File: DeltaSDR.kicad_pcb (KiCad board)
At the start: 2 copper layers, 100 x 80 mm, 177 parts, among them J1 Conn_01x03_Male, J2 Conn_01x05_Male, J3 Barrel_Jack, J4 USB_A, J5 Conn_Coaxial, J6 Conn_01x02_Male, Q1 BSS123, Q2 BSS123, Q3 BSS123, Q4 BSS123, Q5 BSS123, Q6 BSS123, Q7 MMBT3904, T1 Transformer_1P_SS, T2 Transformer_1P_SS, U1 TC1262-33, U10 TLV2464CD, U11 SN74CBT3253, U12 MMG3H21NT1, U2 Si570, U3 SN74CBT3253, U4 PCM3060, U5 CY8C3246PVI-147, U6 TC1262-5, U7 TC1262-5, U8 74HC74, U9 LT6231CSB, Y1 Crystal_GND24

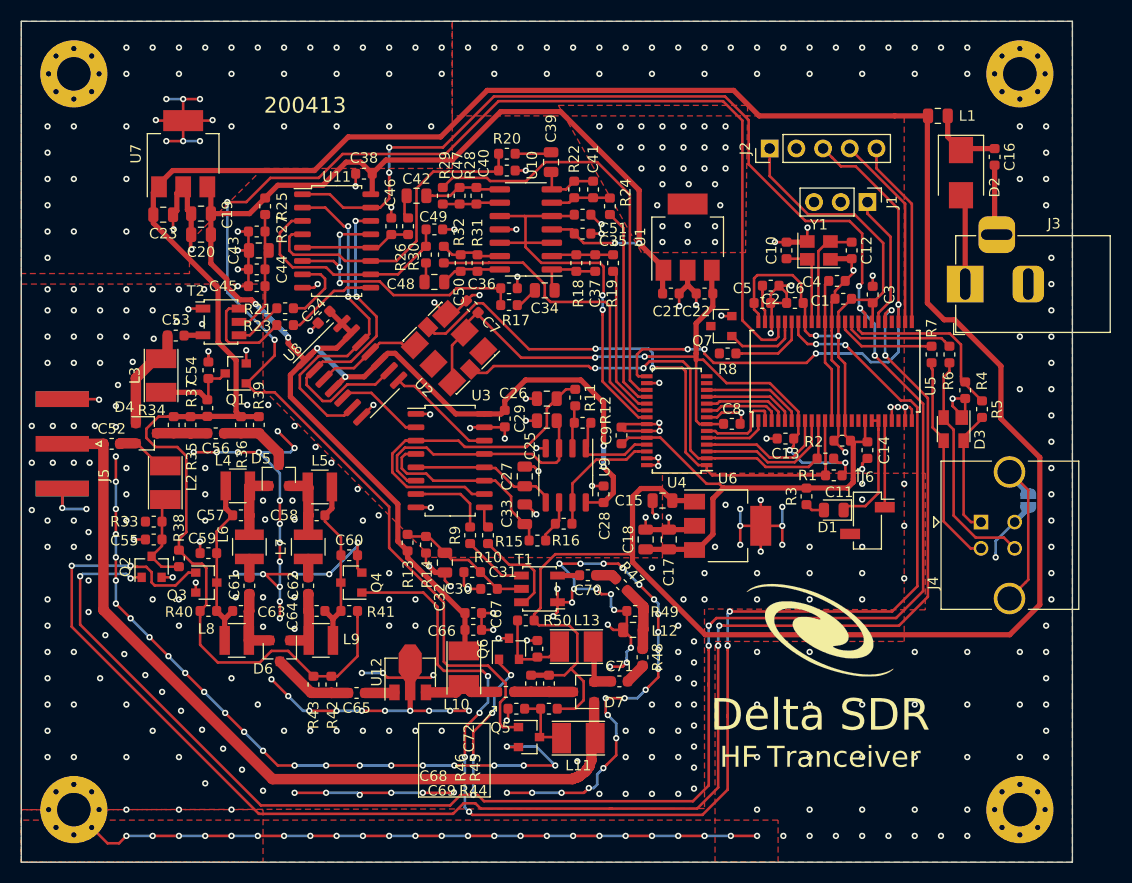
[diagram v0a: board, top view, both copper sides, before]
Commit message: PCM3060 suplied from different voltage rail. Improved ground separation and USB layout
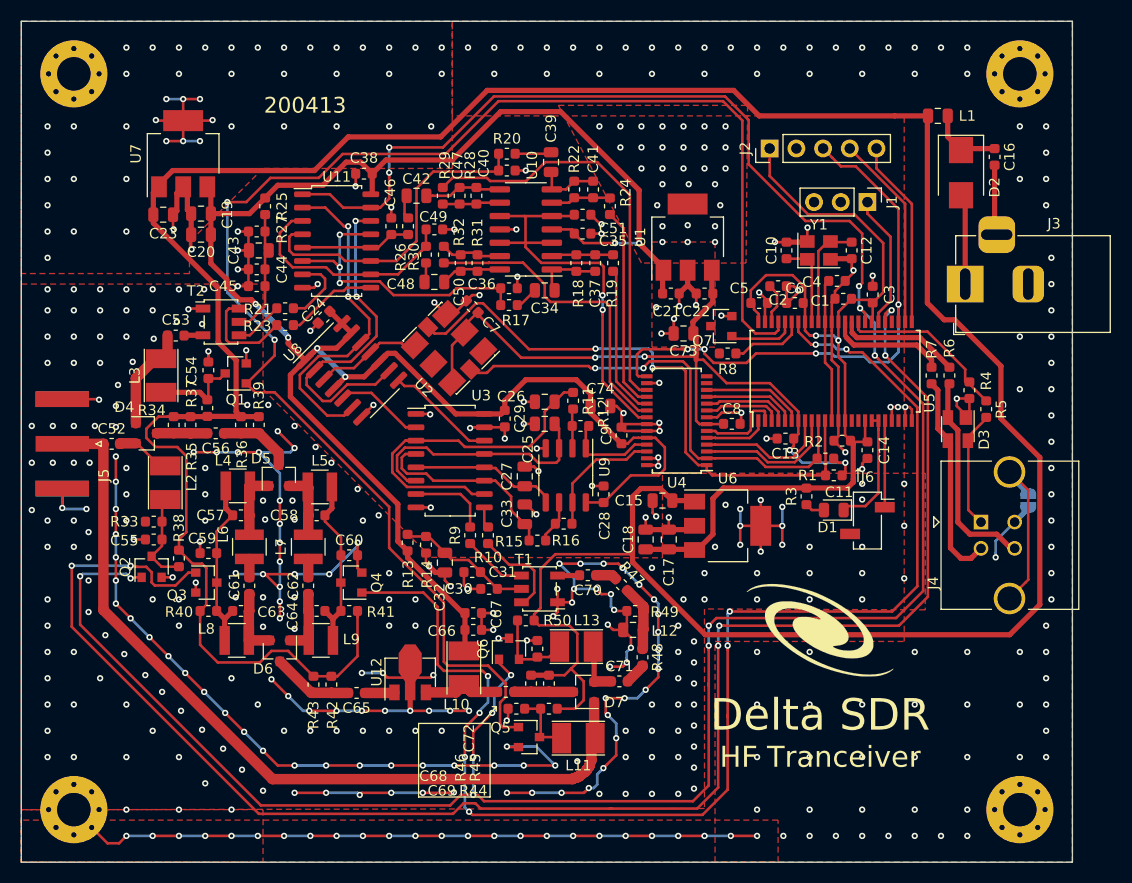
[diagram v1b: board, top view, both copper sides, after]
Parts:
- added C73: 10u, Capacitor_SMD:C_0805_2012Metric, F.Cu at (173.0, 89.7)
- added C74: 10u, Capacitor_SMD:C_0805_2012Metric, F.Cu at (165.1, 96.6)
- moved R6 2.00 mm to (198.3, 93.7)
- moved R7 2.00 mm to (196.6, 93.7)
- moved C2 0.70 mm to (182.0, 85.2)
- moved D3 0.40 mm to (199.1, 98.8)
- moved R5 0.40 mm to (201.8, 96.9)
- moved R4 0.40 mm to (200.2, 95.1)
- moved R12 0.36 mm to (163.2, 98.5)
- moved C25 0.36 mm to (159.8, 98.3)
- moved C26 0.36 mm to (159.8, 96.2)
- moved R11 0.36 mm to (162.5, 96.1)
- moved C5 0.30 mm to (180.2, 86.8)
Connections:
- net KEY_0 renamed Net-(U5-Pad15)
- net KEY_1 renamed Net-(U5-Pad16)
- net Net-(D3-Pad2) renamed /D+
- net Net-(D3-Pad3) renamed /D-
- net RF_BIT renamed Net-(R33-Pad2)
- C9 pad 1: +5VD -> +5V
- U4 pad 24: +5VD -> +5V
- U5 pad 46: GND -> Net-(C2-Pad1)
- U5 pad 47: Net-(C2-Pad1) -> GND
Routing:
- net +5VD: track 102.5 -> 90.5 mm
- net +5V: track 183.2 -> 191.3 mm, vias 8 -> 6
- net GND: track 511.2 -> 515.0 mm, vias 516 -> 520
- net /D+: track 22.3 -> 20.1 mm
- net USB-: track 9.63 -> 11.2 mm
- net USBV+: track 17.1 -> 16.1 mm
- net USB+: track 10.7 -> 11.6 mm
- net ATU_1: track 7.35 -> 6.44 mm
- net HI_TX: track 146.8 -> 145.9 mm
- net Net-(D3-Pad4): track 11.9 -> 11.2 mm
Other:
- net class usb added: clearance 0.2, trace_width 0.4, via_dia 0.6, via_drill 0.3

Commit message: Release. Generated gerbers and BOM
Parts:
- moved R4 1.00 mm to (201.0, 94.5), turned to 180 degrees
- moved C23 0.10 mm to (123.5, 78.3)
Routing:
- net GND: track 515.0 -> 513.0 mm
- net USBV+: track 16.1 -> 17.1 mm
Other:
- board text added: "200417"
- board text removed: "200413"

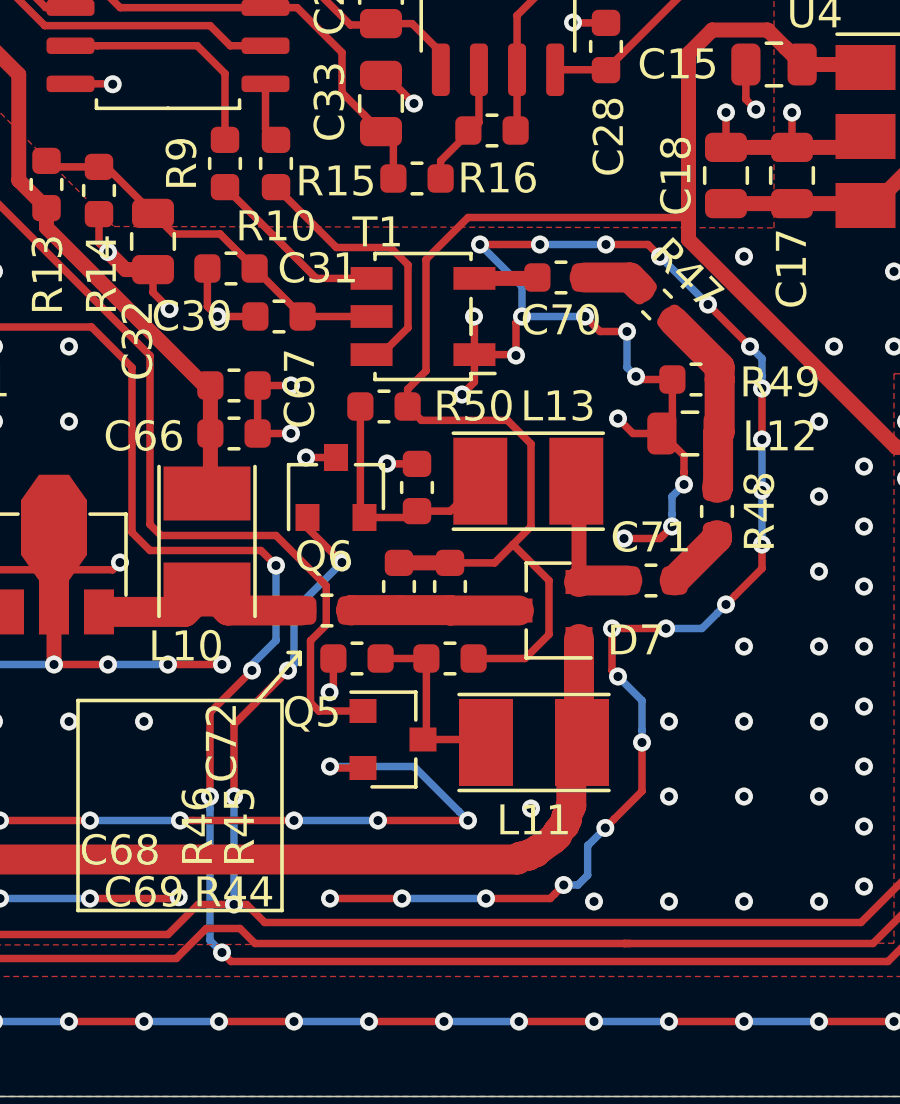
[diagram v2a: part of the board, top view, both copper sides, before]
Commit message: Corrected Q6 connection, RX schematic clean up
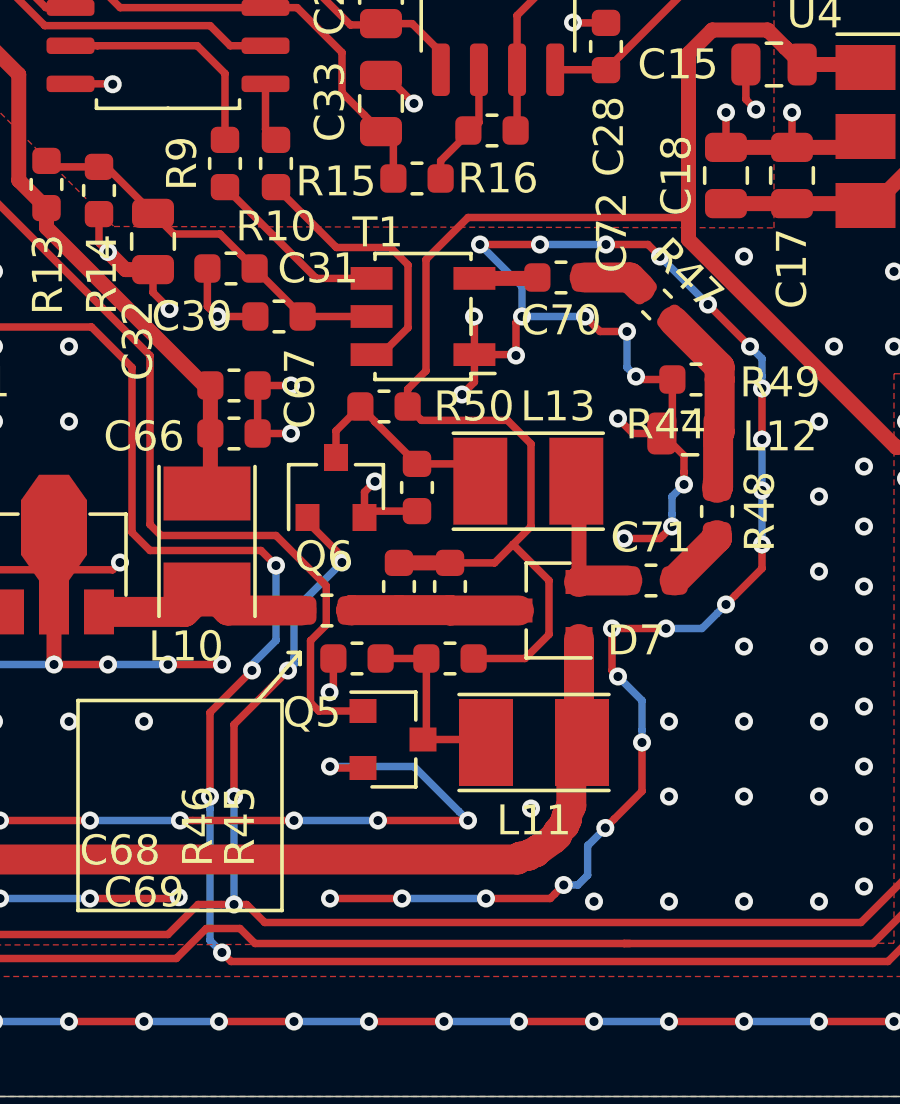
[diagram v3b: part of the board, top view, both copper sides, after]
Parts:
- turned C72 to 270 degrees
- turned R44 to 0 degrees
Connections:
- Q6 pad 2: Net-(C72-Pad1) -> GND
- Q6 pad 3: GND -> Net-(C72-Pad1)
- R44 pad 1: +12V -> Net-(C69-Pad2)
- R44 pad 2: Net-(C69-Pad2) -> +12V
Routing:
- net GND: track 513.0 -> 514.2 mm, vias 520 -> 519
- net Net-(C72-Pad1): track 8.12 -> 7.08 mm

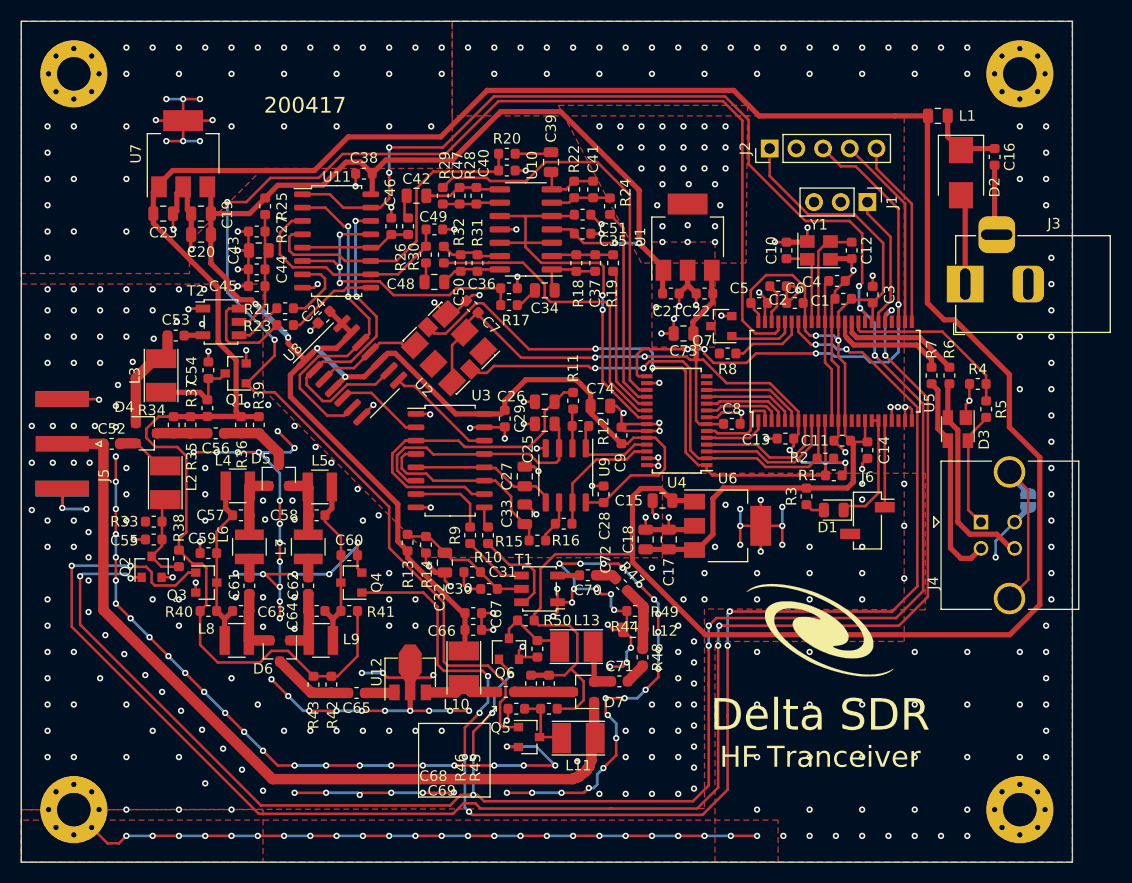
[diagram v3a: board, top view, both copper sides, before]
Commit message: Changed mixers footprints, added 3D models, silk screen correction
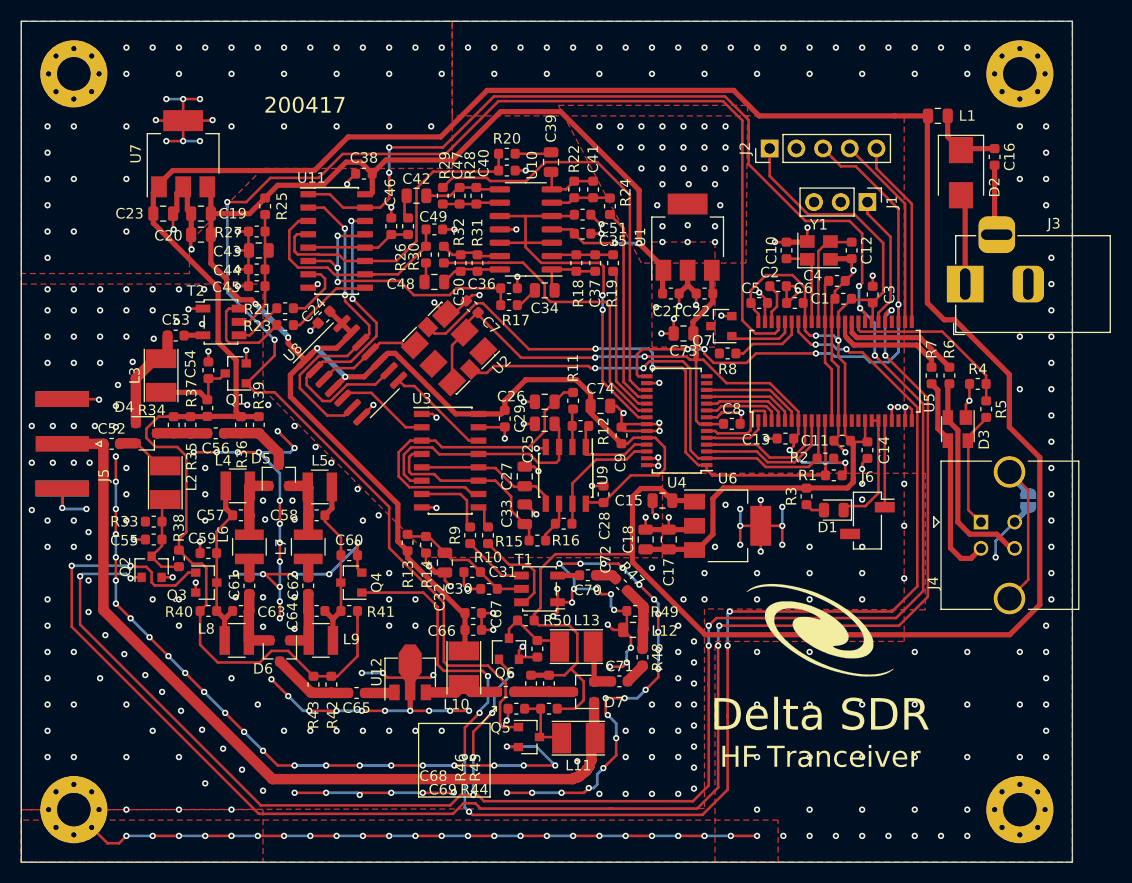
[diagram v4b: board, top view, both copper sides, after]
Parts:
- U11, U3: footprint Package_SO:SOIC-16_4.55x10.3mm_P1.27mm -> Package_SO:SOIC-16_3.9x9.9mm_P1.27mm
- U9: footprint Package_SO:SO-8_3.9x4.9mm_P1.27mm -> Package_SO:SOIC-8_3.9x4.9mm_P1.27mm
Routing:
- net Net-(C49-Pad1): track 22.4 -> 21.0 mm
- net Net-(C33-Pad2): track 19.0 -> 17.9 mm
- net GND: track 514.2 -> 513.1 mm, vias 519 -> 518
- net Net-(C25-Pad2): track 23.7 -> 22.7 mm
- net Net-(C40-Pad1): track 31.1 -> 30.1 mm
- net Net-(C26-Pad2): track 32.6 -> 31.7 mm
- net QSE_Q: track 31.9 -> 32.5 mm

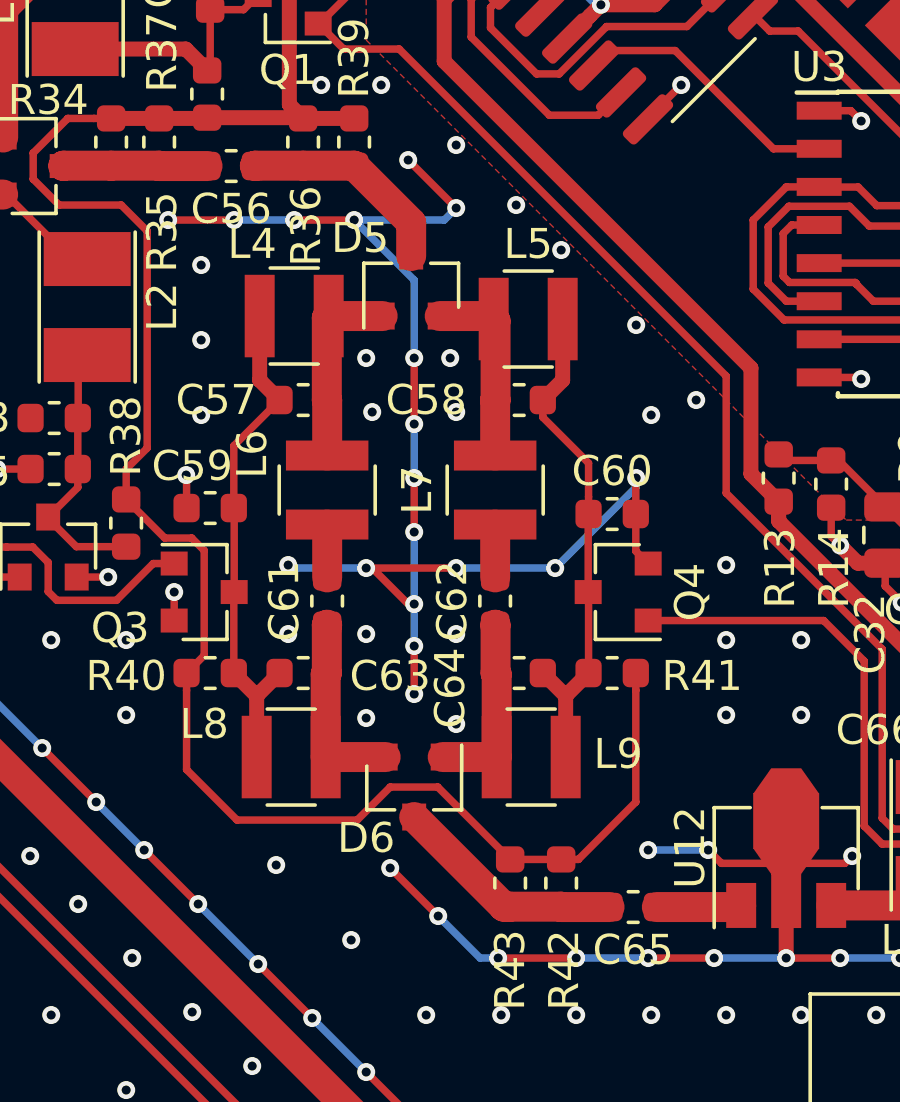
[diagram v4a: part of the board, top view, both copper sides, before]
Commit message: Improved band pass filter layout
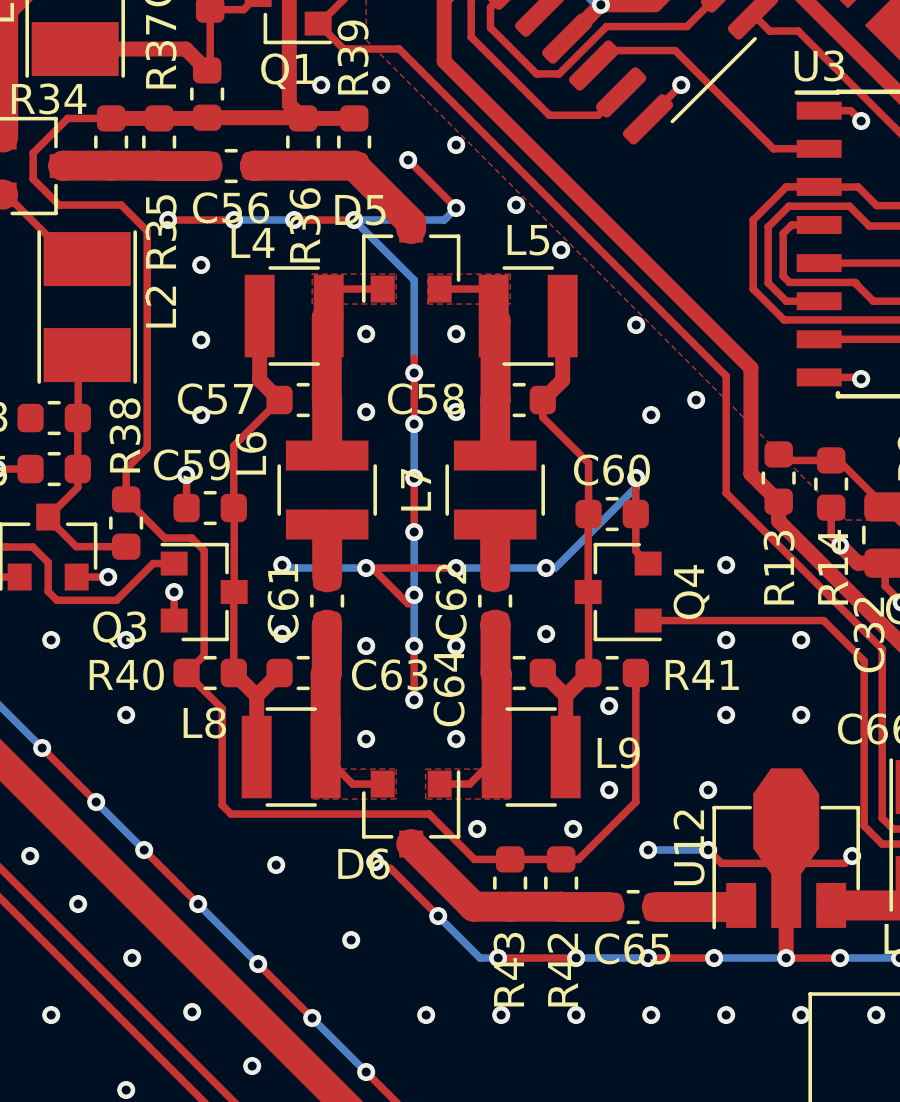
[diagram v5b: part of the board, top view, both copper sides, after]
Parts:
- moved D6 0.91 mm to (134.5, 120.8)
- moved D5 0.90 mm to (134.5, 102.3)
- moved L5 0.10 mm to (138.4, 104.2)
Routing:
- net Net-(C57-Pad1): track 6.48 -> 7.48 mm
- net +12V: track 303.3 -> 302.4 mm
- net Net-(C56-Pad1): track 7.12 -> 6.22 mm
- net Net-(C58-Pad1): track 6.42 -> 7.28 mm
- net GND: vias 518 -> 524
- added copper zone on F.Cu, net Net-(C57-Pad1)
- added copper zone on F.Cu, net Net-(C58-Pad1)
- added copper zone on F.Cu, net Net-(C61-Pad1)
- added copper zone on F.Cu, net Net-(C62-Pad1)
